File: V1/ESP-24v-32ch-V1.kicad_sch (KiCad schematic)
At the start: 8 parts, among them J1 DB141V-2.54-8P, J2 DB141V-2.54-8P, J3 DB141V-2.54-8P, J4 DB141V-2.54-8P, J5 DB141V-2.54-8P, J6 DB141V-2.54-8P, J7 DB141V-2.54-8P, J8 DB141V-2.54-8P

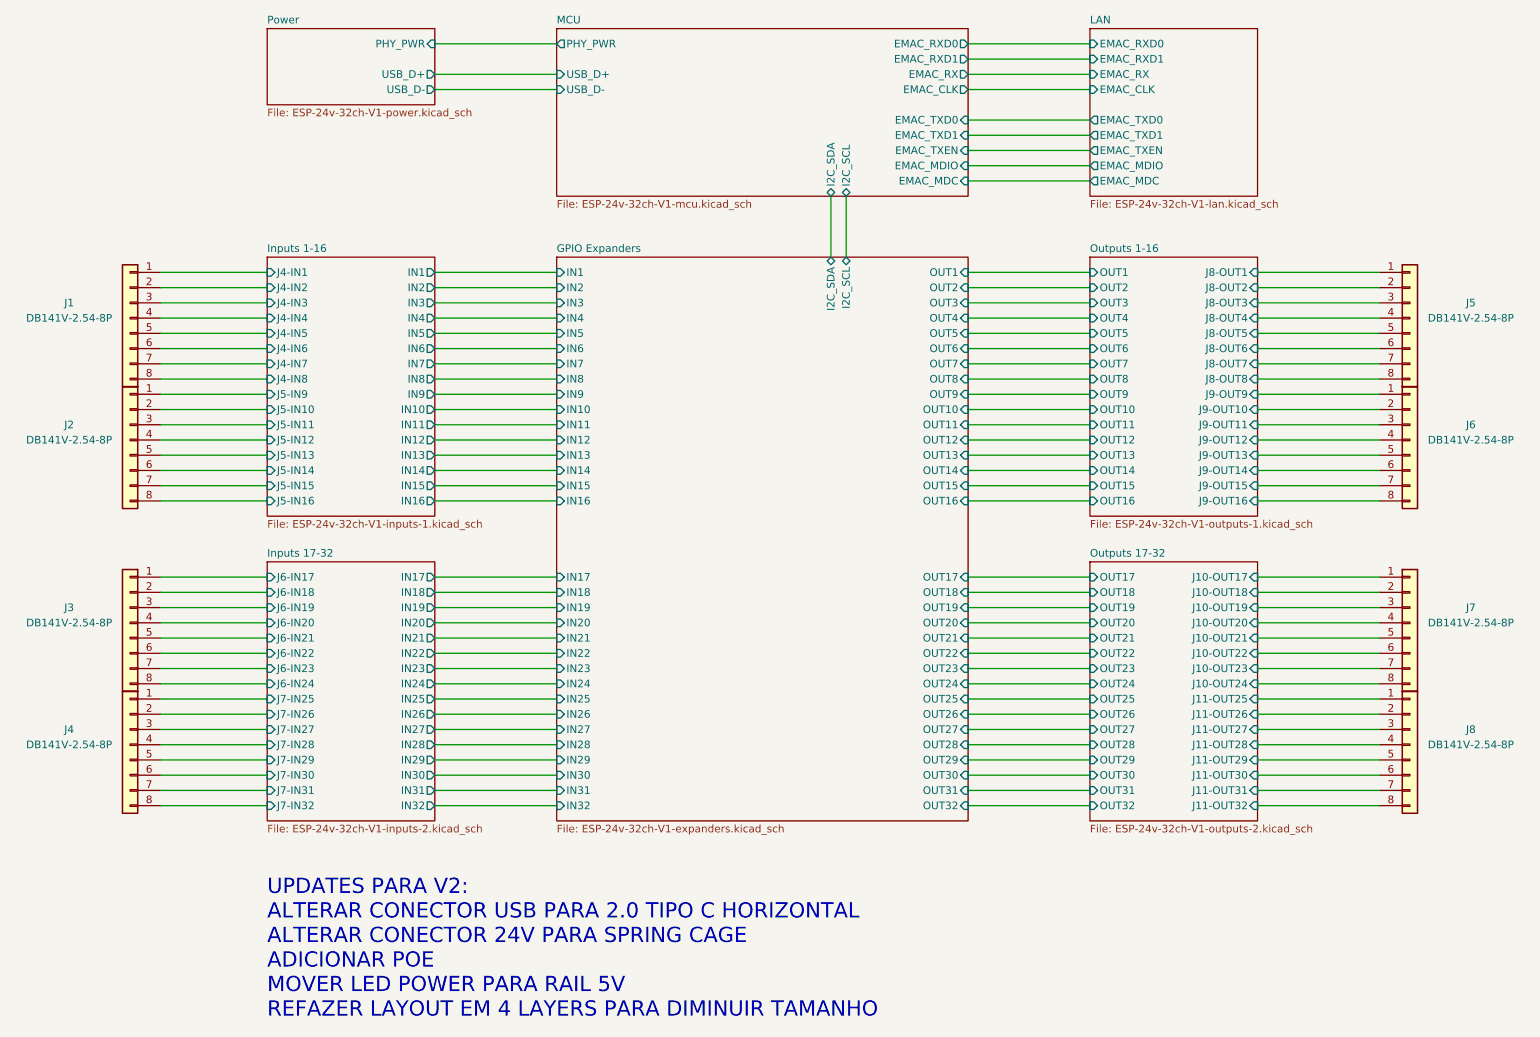
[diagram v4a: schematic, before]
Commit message: Renamed to lowercase
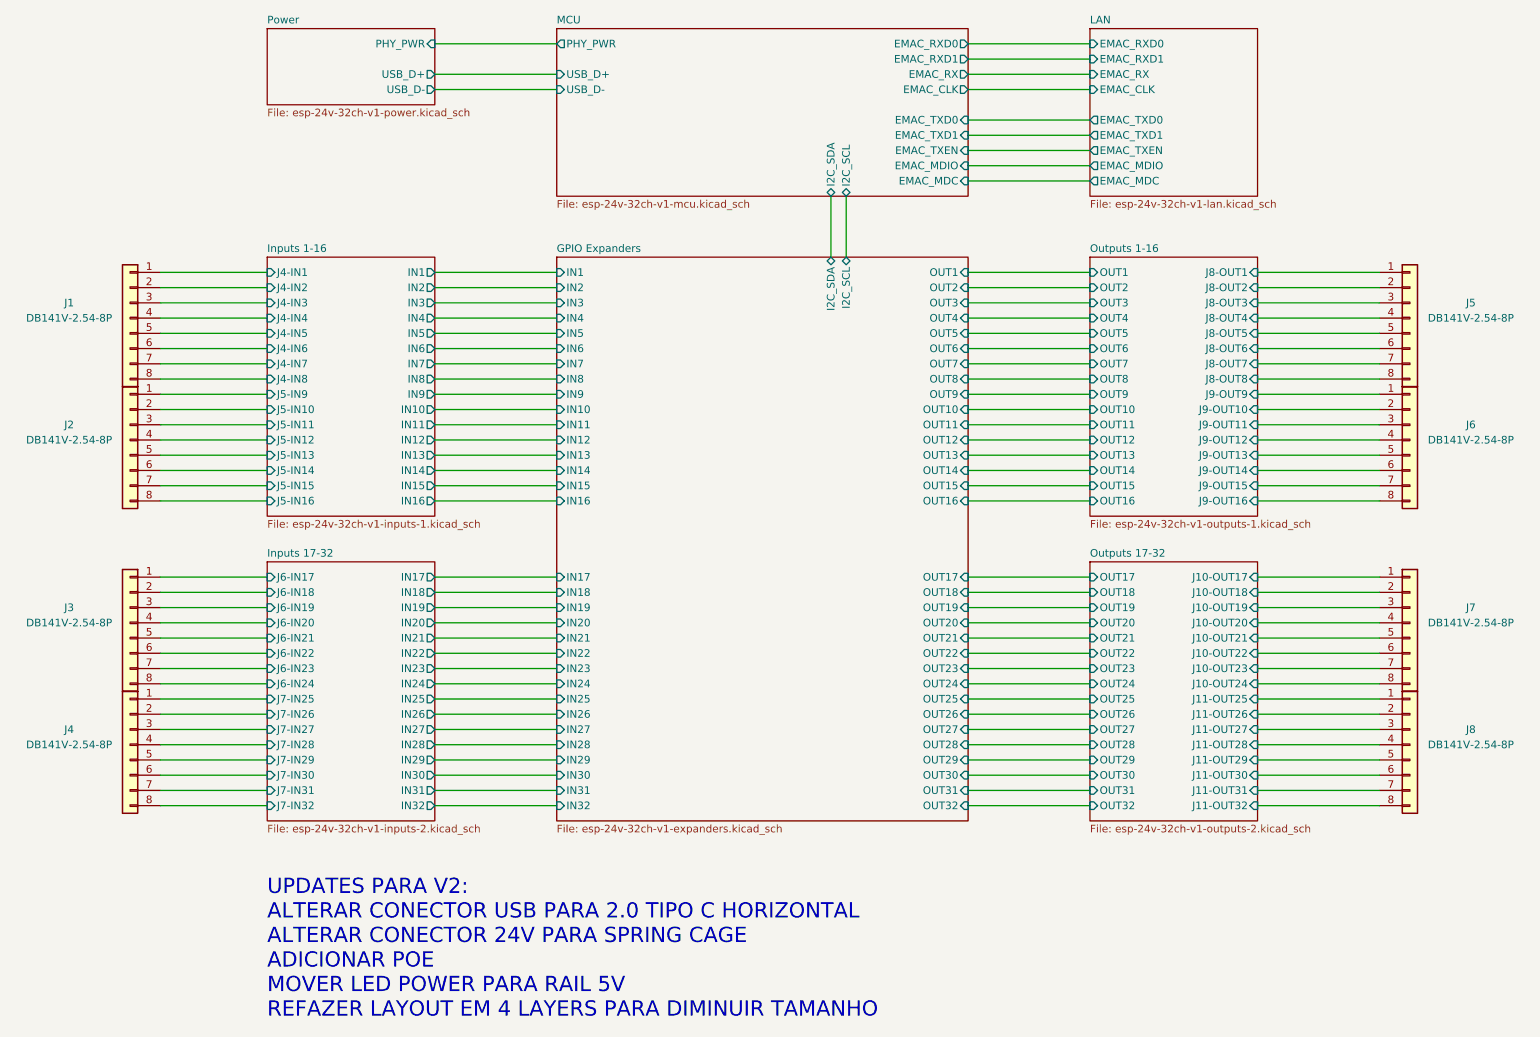
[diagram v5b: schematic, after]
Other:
- sheet GPIO Expanders: file ESP-24v-32ch-V1-expanders.kicad_sch -> esp-24v-32ch-v1-expanders.kicad_sch
- sheet Inputs 1-16: file ESP-24v-32ch-V1-inputs-1.kicad_sch -> esp-24v-32ch-v1-inputs-1.kicad_sch
- sheet Inputs 17-32: file ESP-24v-32ch-V1-inputs-2.kicad_sch -> esp-24v-32ch-v1-inputs-2.kicad_sch
- sheet LAN: file ESP-24v-32ch-V1-lan.kicad_sch -> esp-24v-32ch-v1-lan.kicad_sch
- sheet MCU: file ESP-24v-32ch-V1-mcu.kicad_sch -> esp-24v-32ch-v1-mcu.kicad_sch
- sheet Outputs 1-16: file ESP-24v-32ch-V1-outputs-1.kicad_sch -> esp-24v-32ch-v1-outputs-1.kicad_sch
- sheet Outputs 17-32: file ESP-24v-32ch-V1-outputs-2.kicad_sch -> esp-24v-32ch-v1-outputs-2.kicad_sch
- sheet Power: file ESP-24v-32ch-V1-power.kicad_sch -> esp-24v-32ch-v1-power.kicad_sch
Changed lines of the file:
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@@
     (pin "8")
     (instances
-      (project "ESP-24v-32ch-V1"
+      (project "esp-24v-32ch-v1"
         (path "/2bc5a21a-1d79-419d-a592-6852cc07b00a"
           (reference "J6") (unit 1)
@@
     (pin "8")
     (instances
-      (project "ESP-24v-32ch-V1"
+      (project "esp-24v-32ch-v1"
         (path "/2bc5a21a-1d79-419d-a592-6852cc07b00a"
           (reference "J7") (unit 1)
@@
     (pin "8")
     (instances
-      (project "ESP-24v-32ch-V1"
+      (project "esp-24v-32ch-v1"
         (path "/2bc5a21a-1d79-419d-a592-6852cc07b00a"
           (reference "J5") (unit 1)
@@
     (pin "8")
     (instances
-      (project "ESP-24v-32ch-V1"
+      (project "esp-24v-32ch-v1"
         (path "/2bc5a21a-1d79-419d-a592-6852cc07b00a"
           (reference "J2") (unit 1)
@@
     (pin "8")
     (instances
-      (project "ESP-24v-32ch-V1"
+      (project "esp-24v-32ch-v1"
         (path "/2bc5a21a-1d79-419d-a592-6852cc07b00a"
           (reference "J1") (unit 1)
@@
     (pin "8")
     (instances
-      (project "ESP-24v-32ch-V1"
+      (project "esp-24v-32ch-v1"
         (path "/2bc5a21a-1d79-419d-a592-6852cc07b00a"
           (reference "J8") (unit 1)
@@
     (pin "8")
     (instances
-      (project "ESP-24v-32ch-V1"
+      (project "esp-24v-32ch-v1"
         (path "/2bc5a21a-1d79-419d-a592-6852cc07b00a"
           (reference "J3") (unit 1)
@@
     (pin "8")
     (instances
-      (project "ESP-24v-32ch-V1"
+      (project "esp-24v-32ch-v1"
         (path "/2bc5a21a-1d79-419d-a592-6852cc07b00a"
           (reference "J4") (unit 1)
@@
       (effects (font (size 1.27 1.27)) (justify left bottom))
     )
-    (property "Sheetfile" "ESP-24v-32ch-V1-inputs-2.kicad_sch" (at 60.96 155.5246 0)
+    (property "Sheetfile" "esp-24v-32ch-v1-inputs-2.kicad_sch" (at 60.96 155.5246 0)
       (effects (font (size 1.27 1.27)) (justify left top))
     )
@@
     )
     (instances
-      (project "ESP-24v-32ch-V1"
+      (project "esp-24v-32ch-v1"
         (path "/2bc5a21a-1d79-419d-a592-6852cc07b00a" (page "7"))
       )
@@
       (effects (font (size 1.27 1.27)) (justify left bottom))
     )
-    (property "Sheetfile" "ESP-24v-32ch-V1-outputs-1.kicad_sch" (at 198.12 104.7246 0)
+    (property "Sheetfile" "esp-24v-32ch-v1-outputs-1.kicad_sch" (at 198.12 104.7246 0)
       (effects (font (size 1.27 1.27)) (justify left top))
     )
@@
     )
     (instances
-      (project "ESP-24v-32ch-V1"
+      (project "esp-24v-32ch-v1"
         (path "/2bc5a21a-1d79-419d-a592-6852cc07b00a" (page "8"))
       )
@@
       (effects (font (size 1.27 1.27)) (justify left bottom))
     )
-    (property "Sheetfile" "ESP-24v-32ch-V1-power.kicad_sch" (at 60.96 36.1446 0)
+    (property "Sheetfile" "esp-24v-32ch-v1-power.kicad_sch" (at 60.96 36.1446 0)
       (effects (font (size 1.27 1.27)) (justify left top))
     )
@@
     )
     (instances
-      (project "ESP-24v-32ch-V1"
+      (project "esp-24v-32ch-v1"
         (path "/2bc5a21a-1d79-419d-a592-6852cc07b00a" (page "2"))
       )
@@
       (effects (font (size 1.27 1.27)) (justify left bottom))
     )
-    (property "Sheetfile" "ESP-24v-32ch-V1-inputs-1.kicad_sch" (at 60.96 104.7246 0)
+    (property "Sheetfile" "esp-24v-32ch-v1-inputs-1.kicad_sch" (at 60.96 104.7246 0)
       (effects (font (size 1.27 1.27)) (justify left top))
     )
@@
     )
     (instances
-      (project "ESP-24v-32ch-V1"
+      (project "esp-24v-32ch-v1"
         (path "/2bc5a21a-1d79-419d-a592-6852cc07b00a" (page "6"))
       )
@@
       (effects (font (size 1.27 1.27)) (justify left bottom))
     )
-    (property "Sheetfile" "ESP-24v-32ch-V1-expanders.kicad_sch" (at 109.22 155.5246 0)
+    (property "Sheetfile" "esp-24v-32ch-v1-expanders.kicad_sch" (at 109.22 155.5246 0)
       (effects (font (size 1.27 1.27)) (justify left top))
     )
@@
     )
     (instances
-      (project "ESP-24v-32ch-V1"
+      (project "esp-24v-32ch-v1"
         (path "/2bc5a21a-1d79-419d-a592-6852cc07b00a" (page "5"))
       )
@@
       (effects (font (size 1.27 1.27)) (justify left bottom))
     )
-    (property "Sheetfile" "ESP-24v-32ch-V1-lan.kicad_sch" (at 198.12 51.3846 0)
+    (property "Sheetfile" "esp-24v-32ch-v1-lan.kicad_sch" (at 198.12 51.3846 0)
       (effects (font (size 1.27 1.27)) (justify left top))
     )
@@
     )
     (instances
-      (project "ESP-24v-32ch-V1"
+      (project "esp-24v-32ch-v1"
         (path "/2bc5a21a-1d79-419d-a592-6852cc07b00a" (page "4"))
       )
@@
       (effects (font (size 1.27 1.27)) (justify left bottom))
     )
-    (property "Sheetfile" "ESP-24v-32ch-V1-outputs-2.kicad_sch" (at 198.12 155.5246 0)
+    (property "Sheetfile" "esp-24v-32ch-v1-outputs-2.kicad_sch" (at 198.12 155.5246 0)
       (effects (font (size 1.27 1.27)) (justify left top))
     )
@@
     )
     (instances
-      (project "ESP-24v-32ch-V1"
+      (project "esp-24v-32ch-v1"
         (path "/2bc5a21a-1d79-419d-a592-6852cc07b00a" (page "9"))
       )
@@
       (effects (font (size 1.27 1.27)) (justify left bottom))
     )
-    (property "Sheetfile" "ESP-24v-32ch-V1-mcu.kicad_sch" (at 109.22 51.3846 0)
+    (property "Sheetfile" "esp-24v-32ch-v1-mcu.kicad_sch" (at 109.22 51.3846 0)
       (effects (font (size 1.27 1.27)) (justify left top))
     )
@@
     )
     (instances
-      (project "ESP-24v-32ch-V1"
+      (project "esp-24v-32ch-v1"
         (path "/2bc5a21a-1d79-419d-a592-6852cc07b00a" (page "3"))
       )
